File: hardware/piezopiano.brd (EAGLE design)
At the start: 90 x 99.8 mm, 71 parts, among them J1 CON2, J4 JST-PH-2-SMT-SE, Q1 DMN3404L, Q2 DMN3404L, Q3 DMN3404L, Q4 DMN3404L, Q5 DMN3404L, Q6 DMN3404L, Q7 DMN3404L, Q8 DMN3404L, U1 MEGA48A-AU, U2 CH340E_MSOP10, U3 TP4333, Y1 830069392

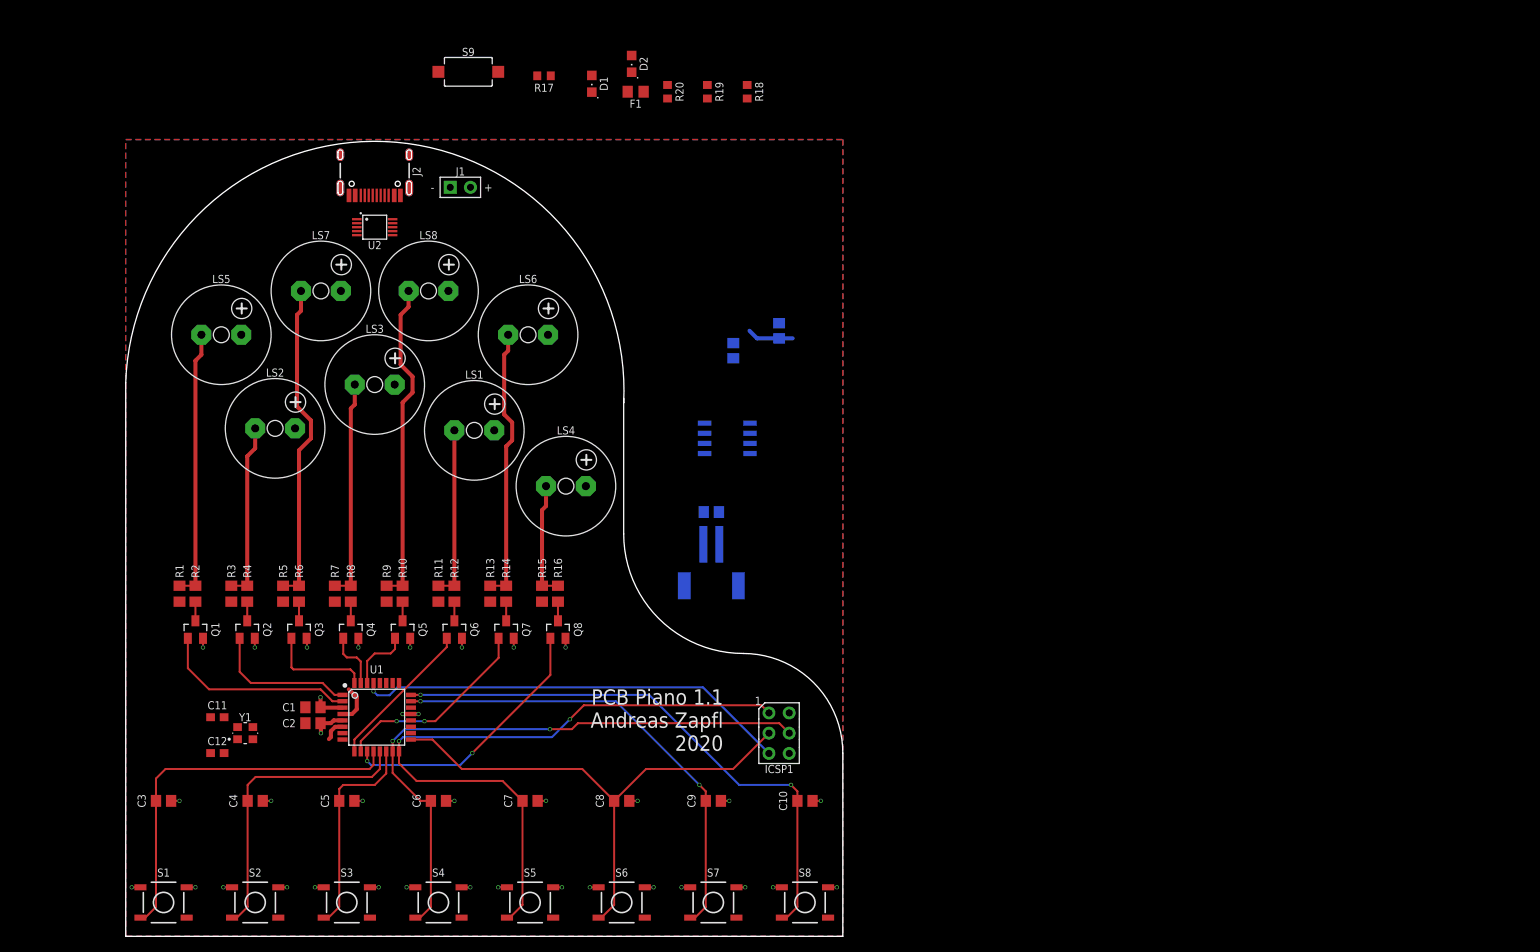
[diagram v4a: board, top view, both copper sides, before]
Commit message: Changed to 328 for Arduino support
Changed to ATmega328
Fixed radius from outline
Corrected CH340E
Changed Pinout 328
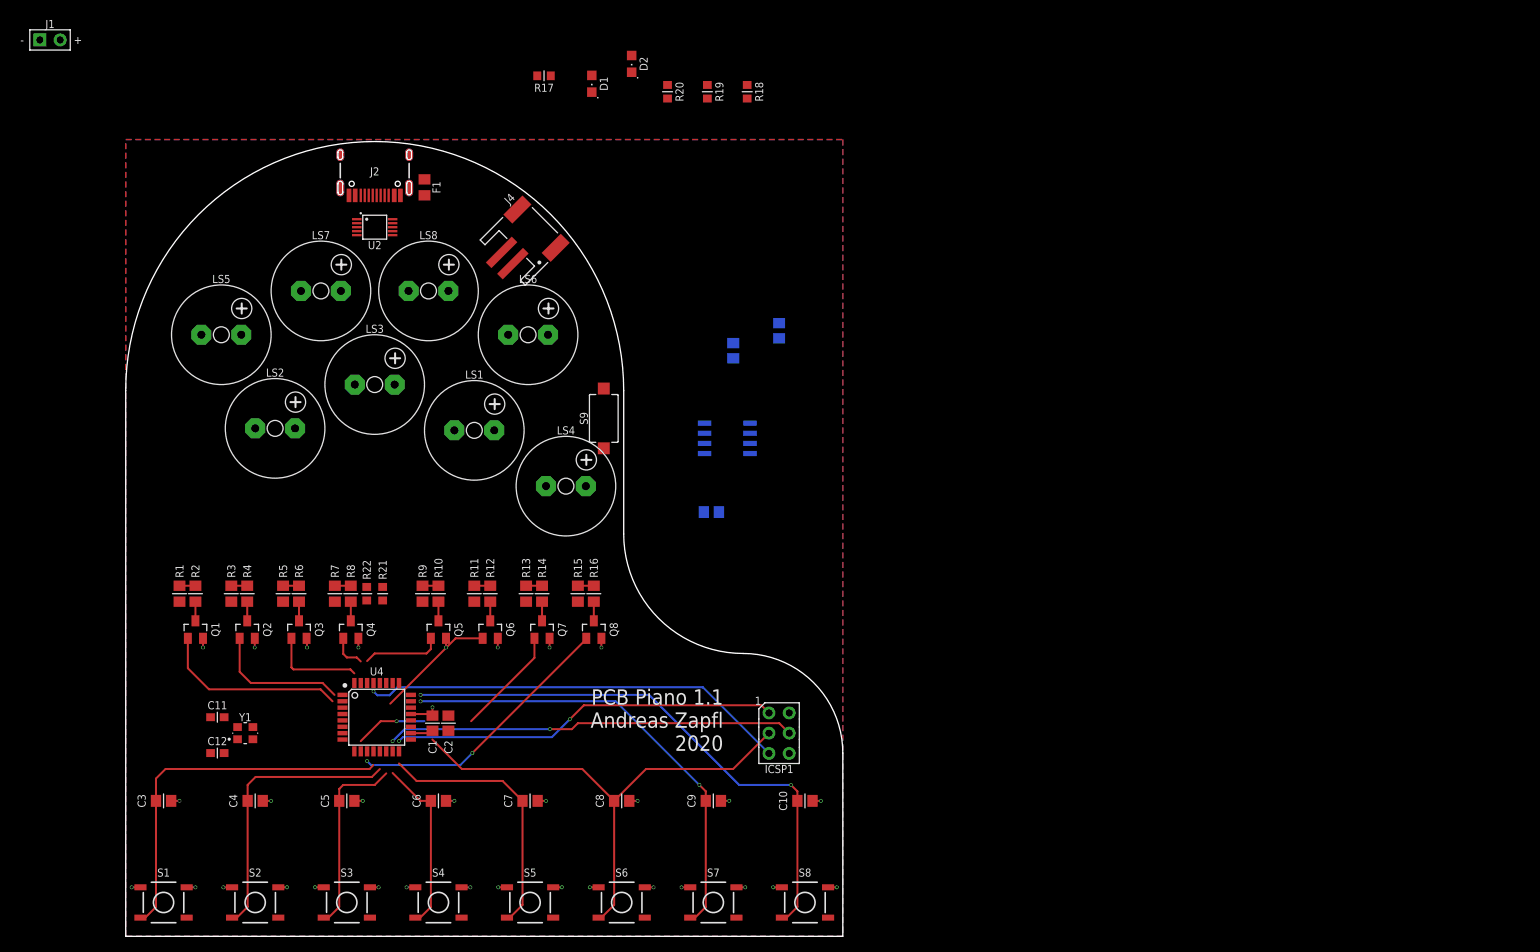
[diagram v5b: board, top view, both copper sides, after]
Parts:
- added R21, R22: 1k, zaan-Resistors:R0603
- U4: value MEGA48A-AU -> MEGA328PB-AU
- moved J1 54.7 mm to (-9.50, 112.5)
- moved J4 48.1 mm to (50.5, 87.8), flipped to the top, turned to 315 degrees
- moved S9 46.7 mm to (60.0, 65.0), turned to 90 degrees
- moved F1 29.1 mm to (37.5, 94.0), turned to 270 degrees
- moved C2 17.0 mm to (40.5, 26.8), turned to 90 degrees
- moved C1 15.1 mm to (38.5, 26.8), turned to 90 degrees
- moved Q5 4.50 mm to (39.2, 38.5)
- moved Q6 4.50 mm to (45.8, 38.5)
- moved Q7 4.50 mm to (52.2, 38.5)
- moved Q8 4.50 mm to (58.8, 38.5)
- moved R10 4.50 mm to (39.2, 43.0)
- moved R11 4.50 mm to (43.8, 43.0)
- moved R12 4.50 mm to (45.8, 43.0)
- moved R13 4.50 mm to (50.2, 43.0)
- moved R14 4.50 mm to (52.2, 43.0)
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- renumbered U1 to U4
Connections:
- net D+ renamed N$31
- net D- renamed N$32
- removed net CC1: J2.A5
- removed net CC2: J2.B5
- new net N$19: R21.1, U4.30
- new net N$20: R22.1, U4.31
- new net N$27: U4.4
- new net N$28: U4.5
- new net N$29: J2.B5, R18.2
- new net N$30: J2.A5, R19.2
- new net RXD: R22.2, U2.9
- new net TXD: R21.2, U2.8
- new net XTAL1: C11.1, U4.7, Y1.1
- new net XTAL2: C12.1, U4.8, Y1.3
- net +5V: no longer U4.4, U4.6
- net GND: now also C11.2, C12.2, R18.1, R19.1, Y1.2, Y1.4; no longer U4.3, U4.5
- net NOTE2: no longer U4.31
- net NOTE5: no longer U4.30
- net T1: no longer U4.15
- net T7: no longer U4.17
- net T8: no longer U4.16
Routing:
- net N$18: track 40.6 -> 2.00 mm
- net N$13: track 40.6 -> 2.00 mm
- net N$16: track 34.4 -> 2.00 mm
- net N$11: track 33.8 -> 2.00 mm
- net N$10: track 27.5 -> 2.00 mm
- net N$4: track 22.2 -> 2.00 mm
- net N$6: track 21.5 -> 2.00 mm
- net N$15: track 14.7 -> 2.00 mm
- net GND: track 45.5 -> 39.2 mm, vias 36 -> 33
- net N$17: track 5.81 -> 0.00 mm
- net +5V: track 7.74 -> 2.83 mm
- net NOTE6: track 19.0 -> 15.0 mm
- net T1: track 77.3 -> 73.3 mm
- net T8: track 84.6 -> 81.8 mm
- net T2: track 26.8 -> 24.0 mm
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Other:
- outline, holes or cut-outs redrawn

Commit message: Test cutout battery connector
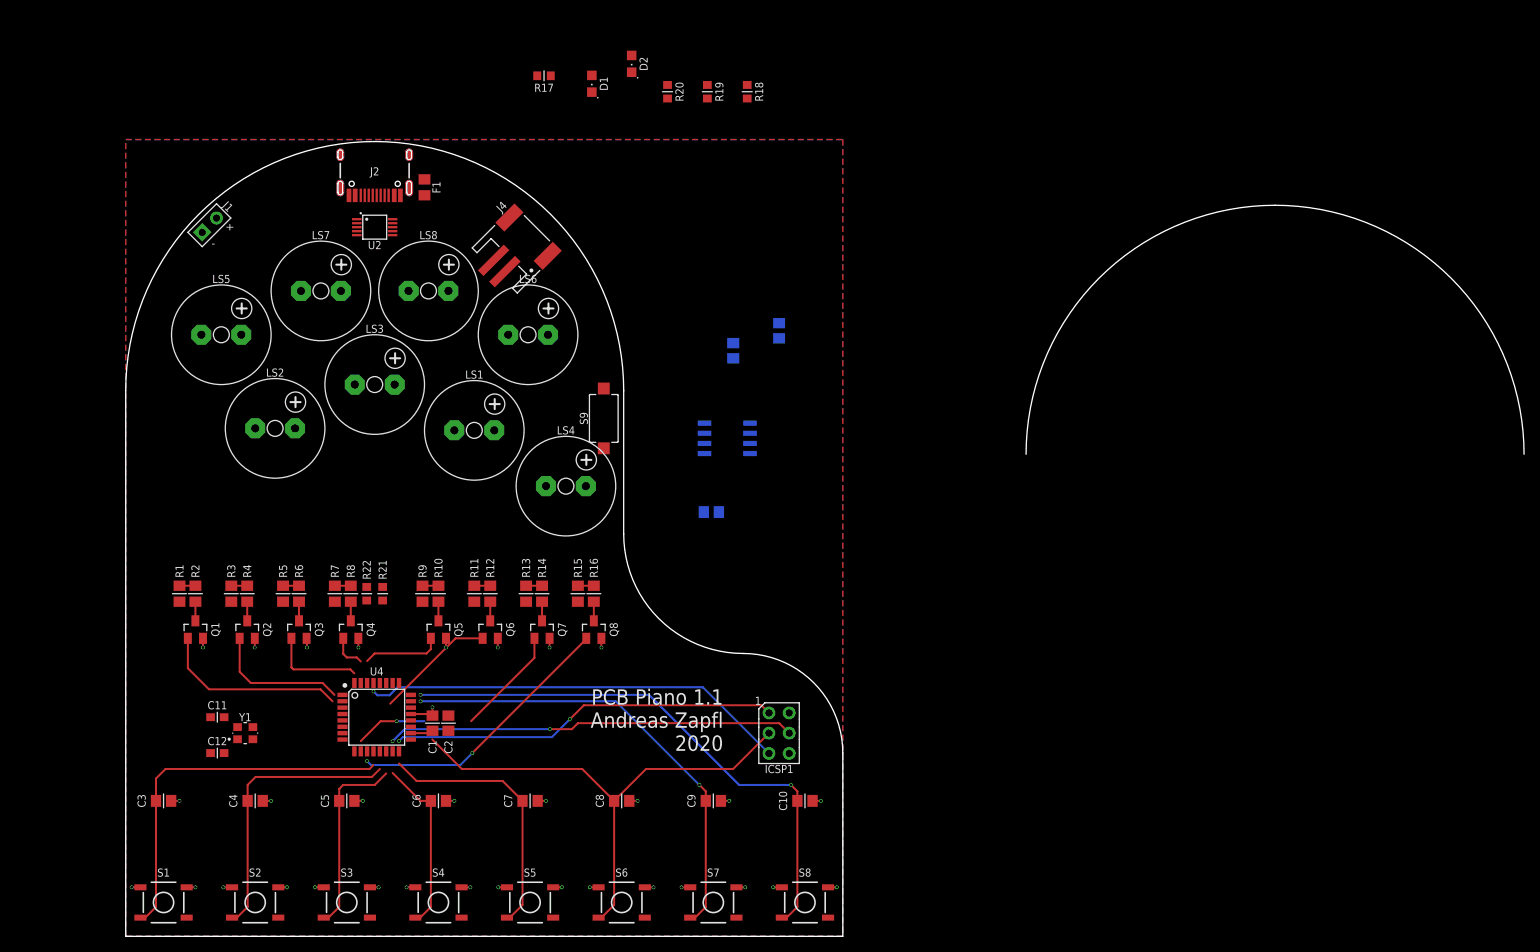
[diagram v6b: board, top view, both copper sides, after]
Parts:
- moved J1 30.7 mm to (10.5, 89.2), turned to 135 degrees
- moved J4 1.41 mm to (49.5, 86.8)
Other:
- board size 90 x 99.8 mm -> 175.5 x 99.8 mm
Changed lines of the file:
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@@
 <layer number="47" name="Measures" color="7" fill="1" visible="no" active="yes"/>
 <layer number="48" name="Document" color="7" fill="1" visible="no" active="yes"/>
-<layer number="49" name="Reference" color="7" fill="1" visible="no" active="yes"/>
+<layer number="49" name="Reference" color="7" fill="1" visible="yes" active="yes"/>
 <layer number="50" name="dxf" color="7" fill="1" visible="no" active="no"/>
 <layer number="51" name="tDocu" color="14" fill="1" visible="yes" active="yes"/>
@@
 <layer number="99" name="SpiceOrder" color="7" fill="1" visible="no" active="no"/>
 <layer number="100" name="Muster" color="7" fill="1" visible="no" active="no"/>
-<layer number="101" name="Patch_Top" color="12" fill="4" visible="no" active="yes"/>
-<layer number="102" name="Vscore" color="7" fill="1" visible="no" active="yes"/>
-<layer number="103" name="tMap" color="7" fill="1" visible="no" active="yes"/>
-<layer number="104" name="Name" color="16" fill="1" visible="no" active="yes"/>
+<layer number="101" name="Patch_Top" color="12" fill="4" visible="yes" active="yes"/>
+<layer number="102" name="Vscore" color="7" fill="1" visible="yes" active="yes"/>
+<layer number="103" name="tMap" color="7" fill="1" visible="yes" active="yes"/>
+<layer number="104" name="Name" color="16" fill="1" visible="yes" active="yes"/>
 <layer number="105" name="tPlate" color="7" fill="1" visible="no" active="yes"/>
 <layer number="106" name="bPlate" color="7" fill="1" visible="no" active="yes"/>
@@
 Andreas Zapfl
 2020</text>
-<text x="-6" y="112.5" size="1.016" layer="21" font="vector" ratio="15" align="center">+</text>
-<text x="-13" y="112.5" size="1.016" layer="21" font="vector" ratio="15" align="center">-</text>
+<text x="13" y="89" size="1.016" layer="21" font="vector" ratio="15" rot="R270" align="center">+</text>
+<text x="11" y="87" size="1.016" layer="21" font="vector" ratio="15" align="center">-</text>
 <wire x1="62" y1="68.5" x2="31.25" y2="68.5" width="0.0762" layer="51"/>
 <wire x1="31.25" y1="68.5" x2="0.5" y2="68.5" width="0.0762" layer="51"/>
 <wire x1="31.25" y1="99.25" x2="31.25" y2="68.5" width="0.0762" layer="51"/>
 <wire x1="31.25" y1="100" x2="31.25" y2="102.75" width="0.0762" layer="51"/>
-<wire x1="0" y1="68.5" x2="62.5" y2="68.5" width="0" layer="20" curve="-180"/>
+<wire x1="0" y1="68.5" x2="31.25" y2="99.75" width="0" layer="20" curve="-90"/>
+<wire x1="31.25" y1="99.75" x2="62.5" y2="68.5" width="0" layer="20" curve="-90"/>
 <wire x1="31.25" y1="68.5" x2="53" y2="90.25" width="0.0762" layer="51"/>
 <wire x1="9.5" y1="90.25" x2="31.25" y2="68.5" width="0.0762" layer="51"/>
@@
 <wire x1="62.5" y1="50.5" x2="77.5" y2="35.5" width="0" layer="51" curve="90"/>
 <wire x1="0" y1="68.5" x2="62.5" y2="68.5" width="0" layer="51" curve="-180"/>
+<wire x1="113" y1="60.5" x2="144.25" y2="91.75" width="0" layer="20" curve="-90"/>
+<wire x1="144.25" y1="91.75" x2="175.5" y2="60.5" width="0" layer="20" curve="-90"/>
+<wire x1="175" y1="60.5" x2="144.25" y2="60.5" width="0.0762" layer="51"/>
+<wire x1="144.25" y1="60.5" x2="113.5" y2="60.5" width="0.0762" layer="51"/>
+<wire x1="144.25" y1="91.25" x2="144.25" y2="60.5" width="0.0762" layer="51"/>
+<wire x1="144.25" y1="60.5" x2="166" y2="82.25" width="0.0762" layer="51"/>
+<wire x1="122.5" y1="82.25" x2="144.25" y2="60.5" width="0.0762" layer="51"/>
+<wire x1="144.25" y1="60.5" x2="166" y2="38.75" width="0.0762" layer="51"/>
+<wire x1="144.25" y1="60.5" x2="144.25" y2="29.75" width="0.0762" layer="51"/>
+<wire x1="165.5" y1="81.75" x2="165.5" y2="83.5" width="0.0762" layer="104"/>
+<wire x1="165.5" y1="81.75" x2="167.25" y2="81.75" width="0.0762" layer="104"/>
 </plain>
 <attributes>
@@
 <attribute name="NAME" x="82" y="21" size="1.016" layer="25" font="vector" ratio="15" align="center"/>
 </element>
-<element name="J1" library="Custom" package="H2-2.54" value="CON2" x="-9.5" y="112.5" smashed="yes" rot="R90">
-<attribute name="NAME" x="-9.5" y="114.5" size="1.016" layer="25" font="vector" ratio="15" align="center"/>
-<attribute name="VALUE" x="-9.5" y="114.75" size="1.016" layer="27" font="vector" ratio="13" rot="R180" align="center"/>
+<element name="J1" library="Custom" package="H2-2.54" value="CON2" x="10.5" y="89.25" smashed="yes" rot="R135">
+<attribute name="NAME" x="12.8357875" y="91.5857875" size="1.016" layer="25" font="vector" ratio="15" rot="R135" align="center"/>
+<attribute name="VALUE" x="8.9090125" y="90.8409875" size="1.016" layer="27" font="vector" ratio="13" rot="R225" align="center"/>
 </element>
 <element name="C100" library="zaan-Capacitors" library_urn="urn:adsk.eagle:library:16758934" package="C0805" package3d_urn="urn:adsk.eagle:package:16758952/3" value="4.7u" x="82" y="76" smashed="yes" rot="MR90">
@@
 <attribute name="VOLTAGE" value="50V" x="11.5" y="23" size="1.778" layer="27" display="off"/>
 </element>
-<element name="J4" library="zaan-Connectors" library_urn="urn:adsk.eagle:library:16759010" package="JST-PH-2-SMT-SE" package3d_urn="urn:adsk.eagle:package:16759071/1" value="JST-PH-2-SMT-SE" x="50.5" y="87.75" smashed="yes" rot="R315">
-<attribute name="DESCRIPTION" value="JST-PH Header" x="50.5" y="87.75" size="1.778" layer="27" rot="R315" display="off"/>
-<attribute name="MF" value="JST" x="50.5" y="87.75" size="1.778" layer="27" rot="R315" display="off"/>
-<attribute name="MPN" value="S2B-PH-SM4-TB(LF)(SN)" x="50.5" y="87.75" size="1.778" layer="27" rot="R315" display="off"/>
-<attribute name="NAME" x="48.171571875" y="92.578425" size="1.016" layer="25" font="vector" ratio="15" rot="R45" align="center"/>
-<attribute name="PITCH" value="2.0" x="50.5" y="87.75" size="1.778" layer="27" rot="R315" display="off"/>
-<attribute name="POSITIONS" value="2" x="50.5" y="87.75" size="1.778" layer="27" rot="R315" display="off"/>
-<attribute name="VALUE" x="45.55025" y="82.800253125" size="1.016" layer="27" font="vector" ratio="15" rot="R315" align="center"/>
+<element name="J4" library="zaan-Connectors" library_urn="urn:adsk.eagle:library:16759010" package="JST-PH-2-SMT-SE" package3d_urn="urn:adsk.eagle:package:16759071/1" value="JST-PH-2-SMT-SE" x="49.5" y="86.75" smashed="yes" rot="R315">
+<attribute name="DESCRIPTION" value="JST-PH Header" x="49.5" y="86.75" size="1.778" layer="27" rot="R315" display="off"/>
+<attribute name="MF" value="JST" x="49.5" y="86.75" size="1.778" layer="27" rot="R315" display="off"/>
+<attribute name="MPN" value="S2B-PH-SM4-TB(LF)(SN)" x="49.5" y="86.75" size="1.778" layer="27" rot="R315" display="off"/>
+<attribute name="NAME" x="47.171571875" y="91.578425" size="1.016" layer="25" font="vector" ratio="15" rot="R45" align="center"/>
+<attribute name="PITCH" value="2.0" x="49.5" y="86.75" size="1.778" layer="27" rot="R315" display="off"/>
+<attribute name="POSITIONS" value="2" x="49.5" y="86.75" size="1.778" layer="27" rot="R315" display="off"/>
+<attribute name="VALUE" x="44.55025" y="81.800253125" size="1.016" layer="27" font="vector" ratio="15" rot="R315" align="center"/>
 </element>
 <element name="U3" library="zaan-IC-Power" library_urn="urn:adsk.eagle:library:16759262" package="SO8" package3d_urn="urn:adsk.eagle:package:16759279/1" value="TP4333" x="75.5" y="62.5" smashed="yes" rot="MR270">
@@
 <wire x1="63.5" y1="108.45" x2="73" y2="106.85" width="0" layer="19" extent="1-1"/>
 <wire x1="58.5" y1="105.95" x2="63.5" y2="108.45" width="0" layer="19" extent="1-1"/>
-<wire x1="48.590809375" y1="84.426596875" x2="58.5" y2="105.95" width="0" layer="19" extent="1-1"/>
-<wire x1="35.57" y1="93.915" x2="48.590809375" y2="84.426596875" width="0" layer="19" extent="1-1"/>
+<wire x1="35.57" y1="98.095" x2="58.5" y2="105.95" width="0" layer="19" extent="1-1"/>
+<wire x1="35.57" y1="98.095" x2="35.57" y2="98.095" width="0" layer="19" extent="1-16"/>
 <wire x1="35.57" y1="93.915" x2="35.57" y2="93.915" width="0" layer="19" extent="1-16"/>
-<wire x1="35.57" y1="98.095" x2="35.57" y2="98.095" width="0" layer="19" extent="1-16"/>
 <wire x1="26.93" y1="98.095" x2="26.93" y2="98.095" width="0" layer="19" extent="1-16"/>
 <wire x1="26.93" y1="93.915" x2="26.93" y2="93.915" width="0" layer="19" extent="1-16"/>
-<wire x1="34.475" y1="92.99" x2="35.57" y2="93.915" width="0" layer="19" extent="1-1"/>
+<wire x1="34.475" y1="92.99" x2="35.57" y2="93.915" width="0" layer="19" extent="1-16"/>
 <wire x1="28.025" y1="92.99" x2="26.93" y2="93.915" width="0" layer="19" extent="1-16"/>
 <wire x1="40.5" y1="27.7" x2="38.55" y2="27.75" width="0" layer="19" extent="1-1"/>
@@
 <wire x1="12.35" y1="27.5" x2="14.0375" y2="26.2625" width="0" layer="19" extent="1-1"/>
 <wire x1="15.9625" y1="24.7375" x2="14.0375" y2="26.2625" width="0" layer="19" extent="1-1"/>
-<wire x1="60" y1="68.75" x2="48.590809375" y2="84.426596875" width="0" layer="19" extent="1-1"/>
+<wire x1="47.590809375" y1="83.426596875" x2="35.57" y2="93.915" width="0" layer="19" extent="1-16"/>
+<wire x1="60" y1="68.75" x2="47.590809375" y2="83.426596875" width="0" layer="19" extent="1-1"/>
 <wire x1="76.25" y1="72.55" x2="60" y2="68.75" width="0" layer="19" extent="1-16"/>
-<wire x1="-10.77" y1="112.5" x2="26.93" y2="98.095" width="0" layer="19" extent="16-16"/>
 </signal>
 <signal name="NOTE1">
@@
 <contactref element="C101" pad="1"/>
 <wire x1="72.55" y1="53.25" x2="78.35" y2="63.135" width="0" layer="19" extent="16-16"/>
-<wire x1="47.176596875" y1="85.840809375" x2="78.35" y2="63.135" width="0" layer="19" extent="1-16"/>
+<wire x1="46.176596875" y1="84.840809375" x2="78.35" y2="63.135" width="0" layer="19" extent="1-16"/>
 </signal>
 <signal name="N$22">
